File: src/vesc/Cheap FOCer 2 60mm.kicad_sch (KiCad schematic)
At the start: 32 parts, among them J1 Conn_01x02, J3 Conn_01x02, P1 MOTOR1, P2 MOTOR1, P3 MOTOR1, P4 HALL/Encoder, P6 USB_C_Plug_USB2.0

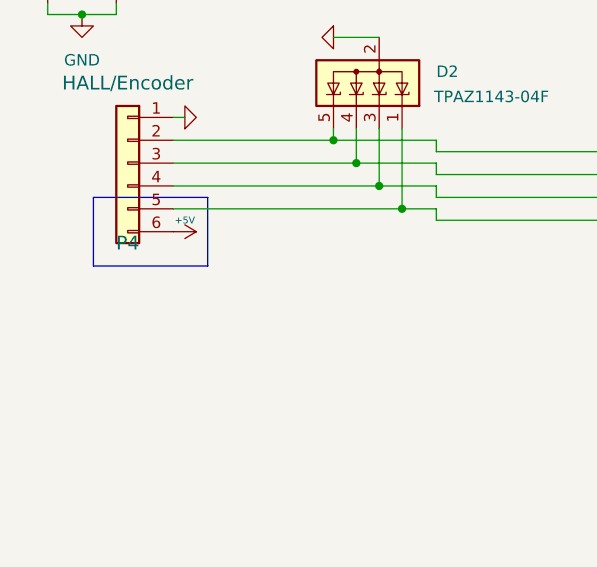
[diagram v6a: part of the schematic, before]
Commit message: decoupling cap for hall sensor
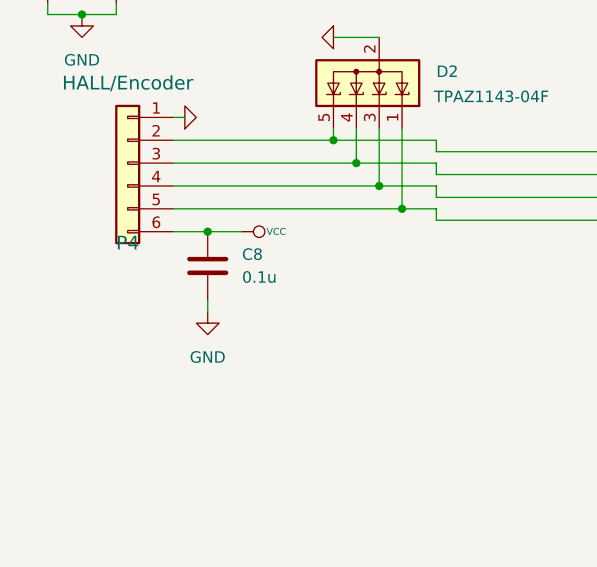
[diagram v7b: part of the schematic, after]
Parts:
- added C8: 0.1u, symbol Device:C
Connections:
- net +5V is gone; now on net VCC: P4.6 (Pin_6)
- net GND: now also C8.2
- net VCC: now also C8.1
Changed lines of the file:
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@@
 	)
 	(rectangle
-		(start 72.39 170.18)
-		(end 85.09 177.8)
-		(stroke
-			(width 0)
-			(type default)
-		)
-		(fill
-			(type none)
-		)
-	)
-	(rectangle
 		(start 78.74 113.03)
 		(end 95.25 116.84)
@@
 		(color 0 0 0 0)
 	)
+	(junction
+		(at 85.09 173.99)
+		(diameter 0)
+		(color 0 0 0 0)
+	)
 	(wire
 		(pts
@@
 	(wire
 		(pts
+			(xy 81.28 173.99) (xy 85.09 173.99)
+		)
+		(stroke
+			(width 0)
+			(type default)
+		)
+	)
+	(wire
+		(pts
 			(xy 236.22 198.12) (xy 236.22 207.01)
 		)
@@
 	(wire
 		(pts
+			(xy 85.09 173.99) (xy 88.9 173.99)
+		)
+		(stroke
+			(width 0)
+			(type default)
+		)
+	)
+	(wire
+		(pts
 			(xy 335.28 142.24) (xy 334.01 142.24)
 		)
@@
 	(wire
 		(pts
+			(xy 85.09 181.61) (xy 85.09 182.88)
+		)
+		(stroke
+			(width 0)
+			(type default)
+		)
+	)
+	(wire
+		(pts
 			(xy 81.28 168.91) (xy 104.14 168.91)
 		)
@@
 	)
 	(symbol
-		(lib_id "BLDC_4-rescue:+5V")
-		(at 81.28 173.99 270)
-		(unit 1)
-		(exclude_from_sim no)
-		(in_bom yes)
-		(on_board yes)
-		(dnp no)
-		(property "Reference" "#PWR06"
-			(at 83.566 173.99 0)
-			(effects
-				(font
-					(size 0.508 0.508)
-				)
-				(hide yes)
-			)
-		)
-		(property "Value" "+5V"
-			(at 82.55 172.72 90)
-			(effects
-				(font
-					(size 0.762 0.762)
-				)
-			)
-		)
-		(property "Footprint" ""
-			(at 81.28 173.99 0)
-			(effects
-				(font
-					(size 1.524 1.524)
-				)
-				(hide yes)
-			)
-		)
-		(property "Datasheet" ""
-			(at 81.28 173.99 0)
-			(effects
-				(font
-					(size 1.524 1.524)
-				)
-				(hide yes)
-			)
-		)
-		(property "Description" ""
-			(at 81.28 173.99 0)
-			(effects
-				(font
-					(size 1.27 1.27)
-				)
-			)
-		)
-		(pin "1"
-		)
-		(instances
-			(project ""
-				(path "/8b53313b-c20e-4d2c-aeda-56c30dbca1c0"
-					(reference "#PWR06")
-					(unit 1)
-				)
-			)
-		)
-	)
-	(symbol
 		(lib_id "BLDC_4-rescue:GND-RESCUE-BLDC_4")
 		(at 82.55 161.29 90)
@@
 	)
 	(symbol
+		(lib_id "power:GND")
+		(at 85.09 182.88 0)
+		(unit 1)
+		(exclude_from_sim no)
+		(in_bom yes)
+		(on_board yes)
+		(dnp no)
+		(fields_autoplaced yes)
+		(property "Reference" "#PWR07"
+			(at 85.09 189.23 0)
+			(effects
+				(font
+					(size 1.27 1.27)
+				)
+				(hide yes)
+			)
+		)
+		(property "Value" "GND"
+			(at 85.09 187.96 0)
+			(effects
+				(font
+					(size 1.27 1.27)
+				)
+			)
+		)
+		(property "Footprint" ""
+			(at 85.09 182.88 0)
+			(effects
+				(font
+					(size 1.27 1.27)
+				)
+				(hide yes)
+			)
+		)
+		(property "Datasheet" ""
+			(at 85.09 182.88 0)
+			(effects
+				(font
+					(size 1.27 1.27)
+				)
+				(hide yes)
+			)
+		)
+		(property "Description" "Power symbol creates a global label with name \"GND\" , ground"
+			(at 85.09 182.88 0)
+			(effects
+				(font
+					(size 1.27 1.27)
+				)
+				(hide yes)
+			)
+		)
+		(pin "1"
+		)
+		(instances
+			(project ""
+				(path "/8b53313b-c20e-4d2c-aeda-56c30dbca1c0"
+					(reference "#PWR07")
+					(unit 1)
+				)
+			)
+		)
+	)
+	(symbol
 		(lib_id "Power_Protection:ESDA5V3SC5")
 		(at 104.14 157.48 180)
@@
 	)
 	(symbol
+		(lib_id "Device:C")
+		(at 85.09 177.8 0)
+		(unit 1)
+		(exclude_from_sim no)
+		(in_bom yes)
+		(on_board yes)
+		(dnp no)
+		(fields_autoplaced yes)
+		(property "Reference" "C8"
+			(at 88.9 176.5299 0)
+			(effects
+				(font
+					(size 1.27 1.27)
+				)
+				(justify left)
+			)
+		)
+		(property "Value" "0.1u"
+			(at 88.9 179.0699 0)
+			(effects
+				(font
+					(size 1.27 1.27)
+				)
+				(justify left)
+			)
+		)
+		(property "Footprint" ""
+			(at 86.0552 181.61 0)
+			(effects
+				(font
+					(size 1.27 1.27)
+				)
+				(hide yes)
+			)
+		)
+		(property "Datasheet" "~"
+			(at 85.09 177.8 0)
+			(effects
+				(font
+					(size 1.27 1.27)
+				)
+				(hide yes)
+			)
+		)
+		(property "Description" "Unpolarized capacitor"
+			(at 85.09 177.8 0)
+			(effects
+				(font
+					(size 1.27 1.27)
+				)
+				(hide yes)
+			)
+		)
+		(pin "2"
+		)
+		(pin "1"
+		)
+		(instances
+			(project ""
+				(path "/8b53313b-c20e-4d2c-aeda-56c30dbca1c0"
+					(reference "C8")
+					(unit 1)
+				)
+			)
+		)
+	)
+	(symbol
 		(lib_id "Connector:USB_C_Plug_USB2.0")
 		(at 74.93 125.73 0)
@@
 					(unit 1)
 				)
+			)
+		)
+	)
+	(symbol
+		(lib_id "BLDC_4-rescue:VCC")
+		(at 88.9 173.99 270)
+		(unit 1)
+		(exclude_from_sim no)
+		(in_bom yes)
+		(on_board yes)
+		(dnp no)
+		(property "Reference" "#PWR06"
+			(at 91.44 173.99 0)
+			(effects
+				(font
+					(size 0.762 0.762)
+				)
+				(hide yes)
+			)
+		)
+		(property "Value" "VCC"
+			(at 92.71 173.99 90)
+			(effects
+				(font
+					(size 0.762 0.762)
+				)
+			)
+		)
+		(property "Footprint" ""
+			(at 88.9 173.99 0)
+			(effects
+				(font
+					(size 1.524 1.524)
+				)
+				(hide yes)
+			)
+		)
+		(property "Datasheet" ""
+			(at 88.9 173.99 0)
+			(effects
+				(font
+					(size 1.524 1.524)
+				)
+				(hide yes)
+			)
+		)
+		(property "Description" ""
+			(at 88.9 173.99 0)
+			(effects
+				(font
+					(size 1.27 1.27)
+				)
+			)
+		)
+		(pin "1"
+		)
+		(instances
+			(project "Cheap FOCer 2 60mm"
+				(path "/8b53313b-c20e-4d2c-aeda-56c30dbca1c0"
+					(reference "#PWR06")
+					(unit 1)
+				)

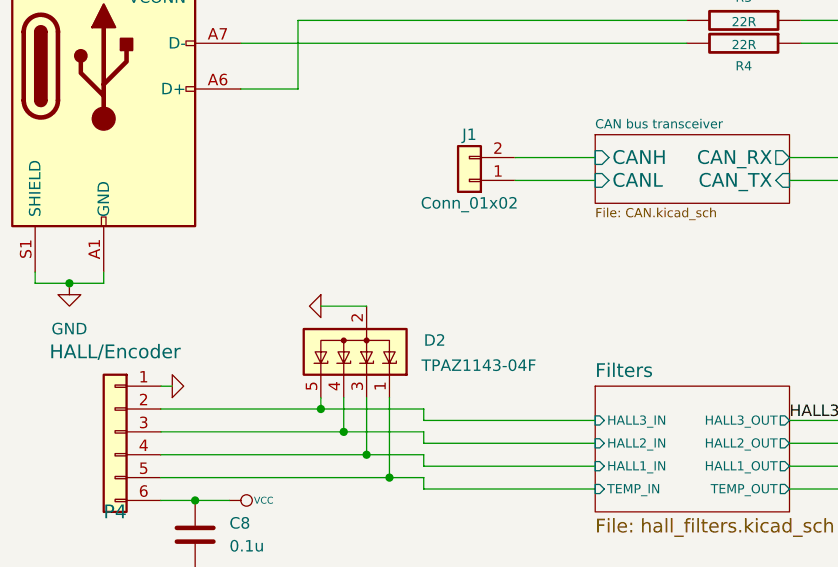
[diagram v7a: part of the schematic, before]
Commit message: changed power MOSFET capacitor ratings
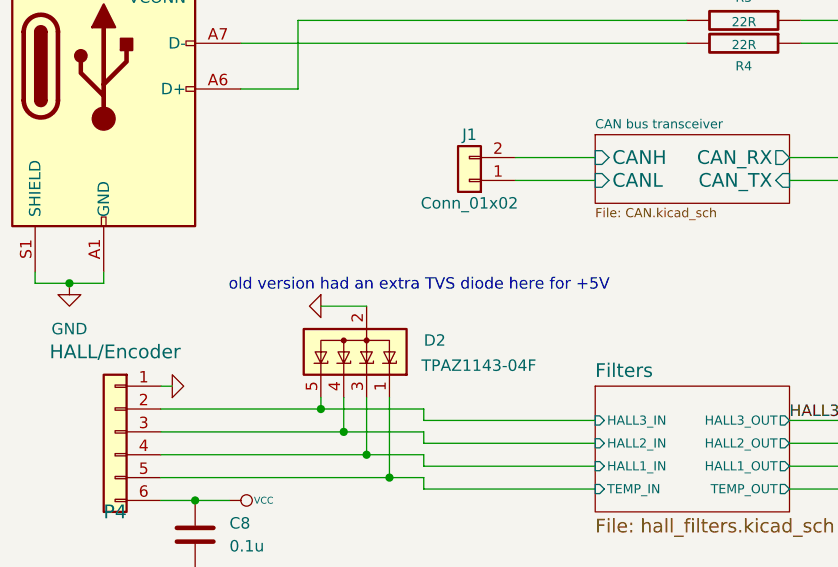
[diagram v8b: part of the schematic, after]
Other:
- note added: "old version had an extra TVS diode here for +5V"
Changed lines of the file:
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@@
+		)
+	)
+	(text "old version had an extra TVS diode here for +5V"
+		(exclude_from_sim no)
+		(at 109.982 150.114 0)
+		(effects
+			(font
+				(size 1.27 1.27)
+			)
 		)
 	)
